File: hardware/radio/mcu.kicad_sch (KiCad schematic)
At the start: 25 parts, among them J202 UART0, SW201 TS-1187A-B-A-B, SW202 TS-1187A-B-A-B, U201 ESP32-S3-MINI-1-N8

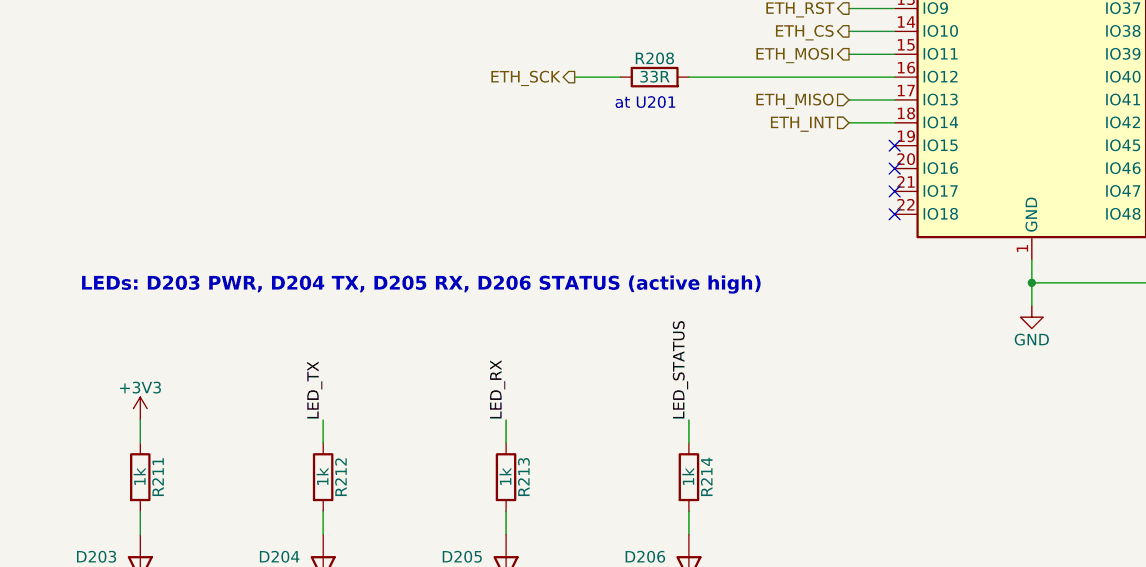
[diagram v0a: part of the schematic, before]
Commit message: fix(hardware): apply the schematic review findings
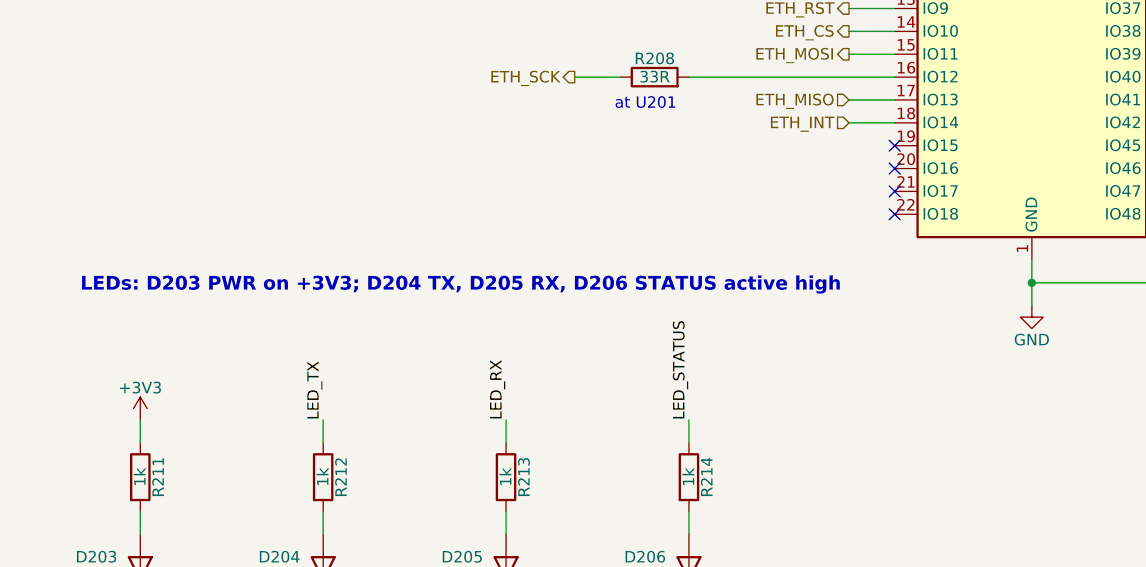
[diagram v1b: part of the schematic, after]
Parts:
- J202: Asm none -> hand
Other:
- note added: "LEDs: D203 PWR on +3V3; D204 TX, D205 RX, D206 STATUS active high"
- note removed: "LEDs: D203 PWR, D204 TX, D205 RX, D206 STATUS (active high)"
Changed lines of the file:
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@@
     (effects (font (size 1.27 1.27)) (justify left bottom))
   )
-  (text "LEDs: D203 PWR, D204 TX, D205 RX, D206 STATUS (active high)"
+  (text "LEDs: D203 PWR on +3V3; D204 TX, D205 RX, D206 STATUS active high"
     (at 105.1 176.45 0)
     (effects (font (size 1.524 1.524) (bold yes)) (justify left bottom))
@@
 			)
 		)
-		(property "Asm" "none"
+		(property "Asm" "hand"
 			(at 340.36 91.44 0)
 			(hide yes)

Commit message: feat(hardware): set up the board stackup, rules and outline
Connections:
- net USB_DN_MCU renamed USB_MCU_DN
- net USB_DP_MCU renamed USB_MCU_DP
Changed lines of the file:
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@@
 		)
 	)
-	(label "USB_DN_MCU"
+	(label "USB_MCU_DN"
 		(at 231.14 124.46 0)
 		(effects
@@
 		)
 	)
-	(label "USB_DP_MCU"
+	(label "USB_MCU_DP"
 		(at 231.14 127 0)
 		(effects
@@
 		)
 	)
-	(label "USB_DN_MCU"
+	(label "USB_MCU_DN"
 		(at 271.78 127 180)
 		(effects
@@
 		)
 	)
-	(label "USB_DP_MCU"
+	(label "USB_MCU_DP"
 		(at 271.78 137.16 180)
 		(effects

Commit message: feat(hardware): move the radio to the ebyte e07 module and fix the power review findings
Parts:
- removed J202: UART0, freedo-radio:PinHeader_1x04_P2.54mm_Vertical, symbol freedo-radio:Conn_01x04
- added J203: GPIO, freedo-radio:PinHeader_1x10_P2.54mm_Vertical, symbol freedo-radio:Conn_01x10
- added R218: 1k, freedo-radio:R_0603_1608Metric, symbol freedo-radio:R
- added R219, R220: 4.7k, freedo-radio:R_0603_1608Metric, symbol freedo-radio:R
- R207: value 510R -> 1k; LCSC C23193 -> C21190; MPN 0603WAF5100T5E -> 0603WAF1001T5E
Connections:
- net +3V3: now also J203.1 (Pin_1), R219.1, R220.1
- net GND: now also J203.10 (Pin_10)
- net UART0_RX: now also R218.1
- net UART0_TX: now also J203.8 (Pin_8)
- net IO7: now reaches U201.11 (IO7)
- net IO7: now also J203.6 (Pin_6)
- net IO8: now reaches U201.12 (IO8)
- net IO8: now also J203.7 (Pin_7)
- net I2C_SDA: now reaches U201.19 (IO15)
- net I2C_SDA: now also J203.2 (Pin_2), R219.2
- net I2C_SCL: now reaches U201.20 (IO16)
- net I2C_SCL: now also J203.3 (Pin_3), R220.2
- net VBUS_SENSE: now reaches U201.21 (IO17)
- net E22_NRST: now reaches U201.25 (IO21)
- net E22_RXEN: now reaches U201.27 (IO47)
- net E22_BUSY: now reaches U201.30 (IO48)
- net IO1: now reaches U201.5 (IO1)
- net IO1: now also J203.4 (Pin_4)
- net IO2: now reaches U201.6 (IO2)
- net IO2: now also J203.5 (Pin_5)
- new net: J203.9 (Pin_9), R218.2
- no-connect marks 19 -> 9
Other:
- note added: "J203 DNP (Asm hand): 1x10 2.54 mm header at a board edge (spec 5.5)."
- note added: "Pin 1 is a 3V3 output: never feed 3V3 into the header."
- note added: "R207 1k at U201 (HDG 1.3.7, review E02)"
- note added: "R219, R220: DNP I2C pull-ups."
- note added: "U0TXD via R207 1k, U0RXD via R218 1k (review E02)."
- note added: "UART0 debug and GPIO header (spec 5.5)"
- note removed: "J202 DNP: fit by hand for log capture. No 3V3 on the header."
- note removed: "R207 at U201 (HDG 1.3.7)"
- note removed: "UART0 debug (spec 5.5)"

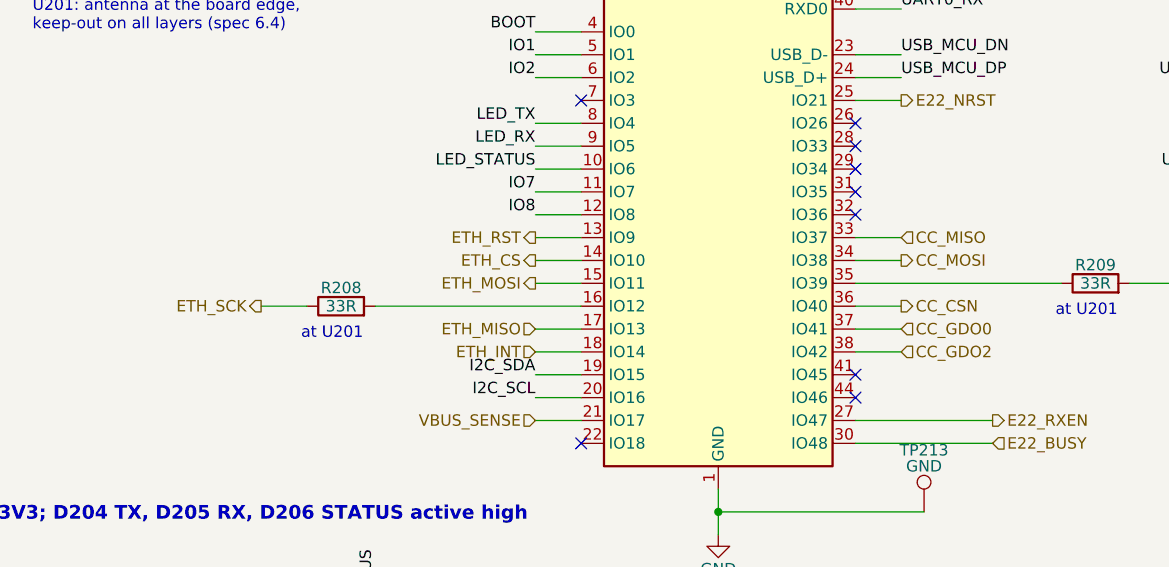
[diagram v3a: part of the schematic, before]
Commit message: feat(hardware): make both spi buses planar and move decoupling to its pins
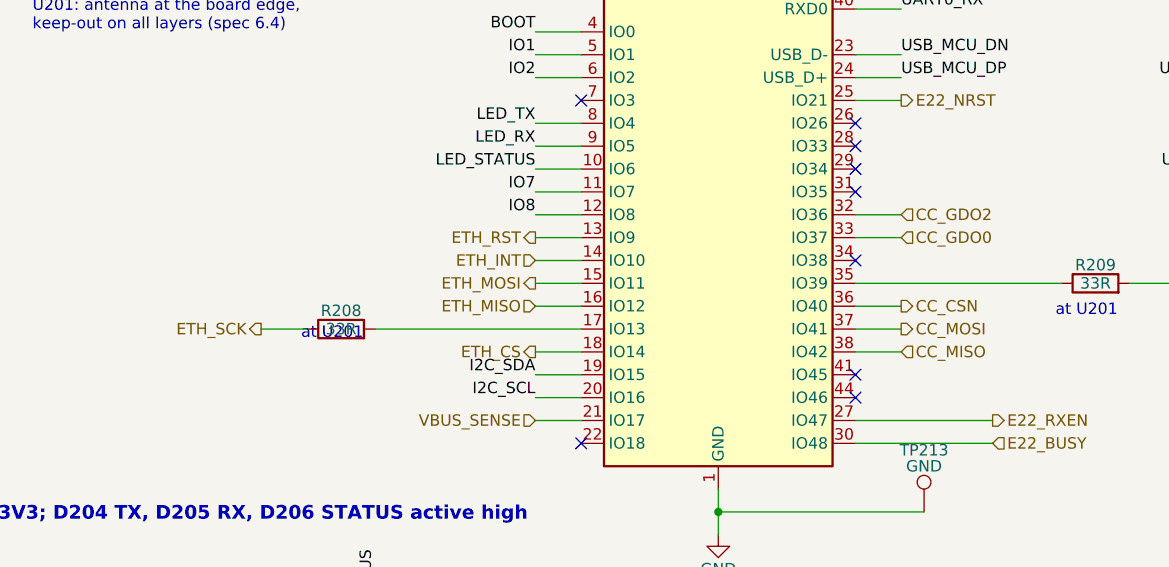
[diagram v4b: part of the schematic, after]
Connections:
- net CC_GDO0: now also U201.33 (IO37); no longer U201.37 (IO41)
- net CC_GDO2: now also U201.32 (IO36); no longer U201.38 (IO42)
- net CC_MISO: now also U201.38 (IO42); no longer U201.33 (IO37)
- net CC_MOSI: now also U201.37 (IO41); no longer U201.34 (IO38)
- net ETH_CS: now also U201.18 (IO14); no longer U201.14 (IO10)
- net ETH_INT: now also U201.14 (IO10); no longer U201.18 (IO14)
- net ETH_MISO: now also U201.16 (IO12); no longer U201.17 (IO13)
- net at R208.2: now also U201.17 (IO13); no longer U201.16 (IO12)
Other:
- moved on the sheet: R208
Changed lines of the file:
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@@
 	)
 	(no_connect
-		(at 226.06 142.24)
+		(at 226.06 147.32)
 	)
 	(no_connect
@@
 	(wire
 		(pts
+			(xy 195.58 154.94)
+			(xy 172.72 154.94)
+		)
+	)
+	(wire
+		(pts
+			(xy 165.1 154.94)
+			(xy 160.02 154.94)
+		)
+	)
+	(wire
+		(pts
 			(xy 195.58 152.4)
-			(xy 172.72 152.4)
-		)
-	)
-	(wire
-		(pts
-			(xy 165.1 152.4)
-			(xy 160.02 152.4)
-		)
-	)
-	(wire
-		(pts
-			(xy 195.58 154.94)
-			(xy 190.5 154.94)
+			(xy 190.5 152.4)
 		)
 	)
@@
 	(wire
 		(pts
-			(xy 226.06 147.32)
-			(xy 231.14 147.32)
+			(xy 226.06 142.24)
+			(xy 231.14 142.24)
 		)
 	)
@@
 	(hierarchical_label "ETH_CS"
 		(shape output)
-		(at 190.5 147.32 180)
+		(at 190.5 157.48 180)
 		(effects
 			(font
@@
 	(hierarchical_label "ETH_SCK"
 		(shape output)
-		(at 160.02 152.4 180)
+		(at 160.02 154.94 180)
 		(effects
 			(font
@@
 	(hierarchical_label "ETH_MISO"
 		(shape input)
-		(at 190.5 154.94 180)
+		(at 190.5 152.4 180)
 		(effects
 			(font
@@
 	(hierarchical_label "ETH_INT"
 		(shape input)
-		(at 190.5 157.48 180)
+		(at 190.5 147.32 180)
 		(effects
 			(font
@@
 	(hierarchical_label "CC_MISO"
 		(shape input)
-		(at 231.14 144.78 0)
+		(at 231.14 157.48 0)
 		(effects
 			(font
@@
 	(hierarchical_label "CC_MOSI"
 		(shape output)
-		(at 231.14 147.32 0)
+		(at 231.14 154.94 0)
 		(effects
 			(font
@@
 	(hierarchical_label "CC_GDO0"
 		(shape input)
-		(at 231.14 154.94 0)
+		(at 231.14 144.78 0)
 		(effects
 			(font
@@
 	(hierarchical_label "CC_GDO2"
 		(shape input)
-		(at 231.14 157.48 0)
+		(at 231.14 142.24 0)
 		(effects
 			(font
@@
 	(symbol
 		(lib_id "freedo-radio:R")
-		(at 168.91 152.4 90)
+		(at 168.91 154.94 90)
 		(unit 1)
 		(in_bom yes)
@@
 		(dnp no)
 		(property "Reference" "R208"
-			(at 168.91 150.368 90)
+			(at 168.91 152.908 90)
 			(effects
 				(font
@@
 		)
 		(property "Value" "33R"
-			(at 168.91 152.4 90)
+			(at 168.91 154.94 90)
 			(effects
 				(font
@@
 		)
 		(property "Footprint" "freedo-radio:R_0603_1608Metric"
-			(at 168.91 152.4 0)
+			(at 168.91 154.94 0)
 			(hide yes)
 			(effects
@@
 		)
 		(property "Datasheet" ""
-			(at 168.91 152.4 0)
+			(at 168.91 154.94 0)
 			(hide yes)
 			(effects
@@
 		)
 		(property "Description" "Resistor"
-			(at 168.91 152.4 0)
+			(at 168.91 154.94 0)
 			(hide yes)
 			(effects
@@
 		)
 		(property "MPN" "0603WAF330JT5E"
-			(at 168.91 152.4 0)
+			(at 168.91 154.94 0)
 			(hide yes)
 			(effects
@@
 		)
 		(property "LCSC" "C23140"
-			(at 168.91 152.4 0)
+			(at 168.91 154.94 0)
 			(hide yes)
 			(effects
@@
 		)
 		(property "Asm" "JLC"
-			(at 168.91 152.4 0)
-			(hide yes)
-			(effects
+			(at 168.91 154.94 0)
+			(hide yes)
+			(effects
